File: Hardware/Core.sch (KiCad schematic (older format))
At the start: 12 parts

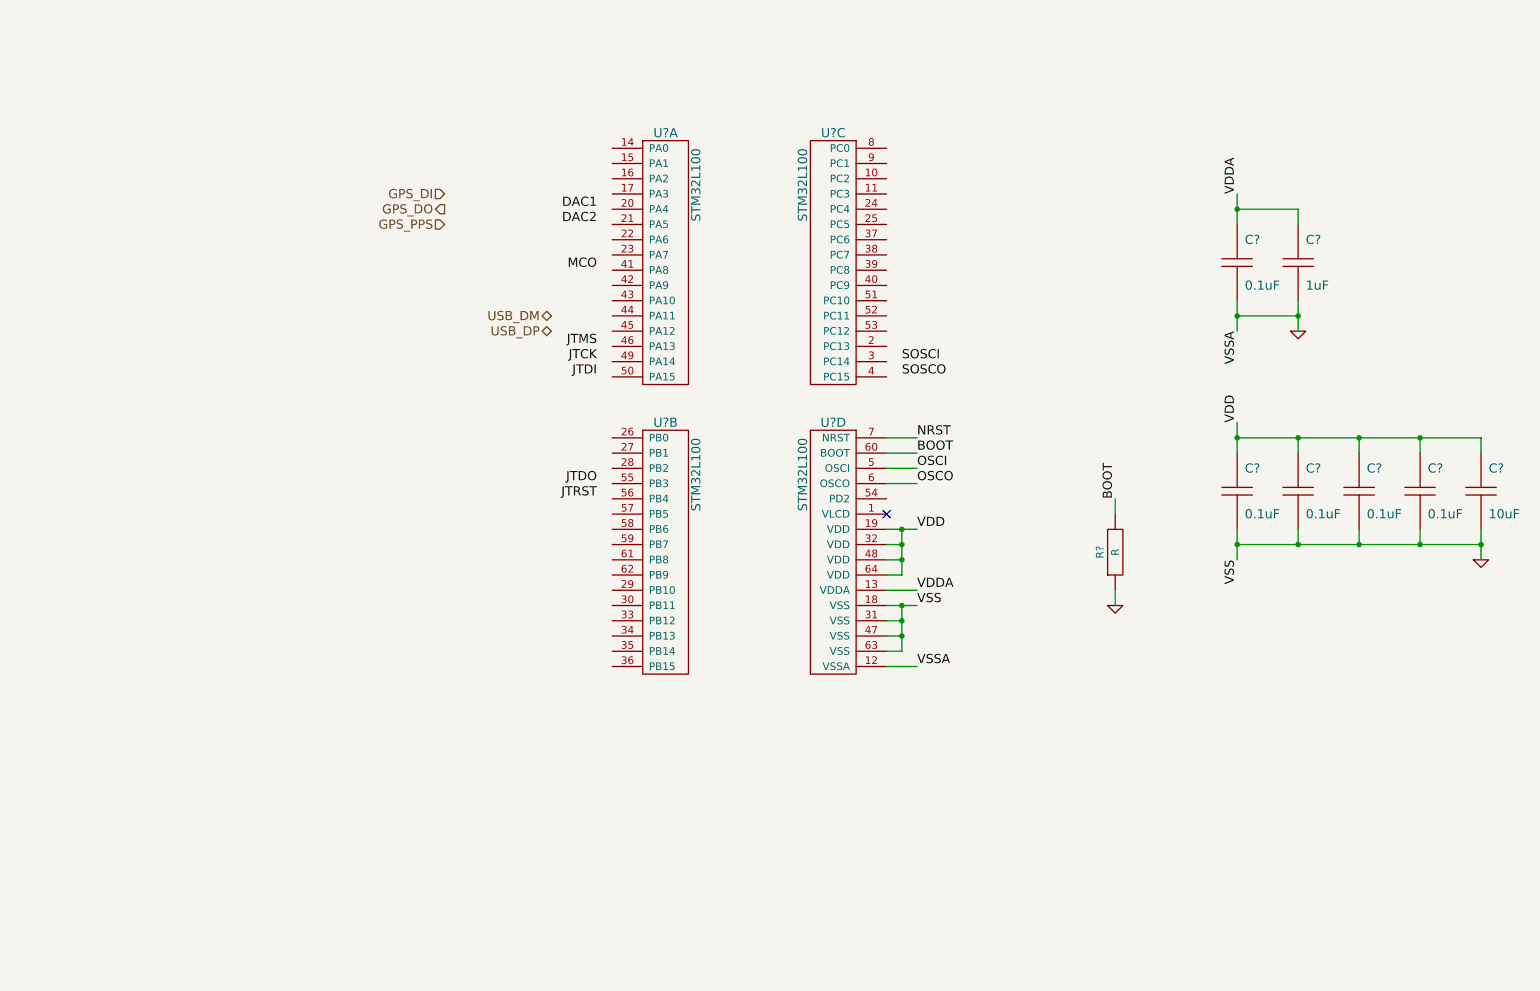
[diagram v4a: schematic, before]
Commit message: Add programming connector to core
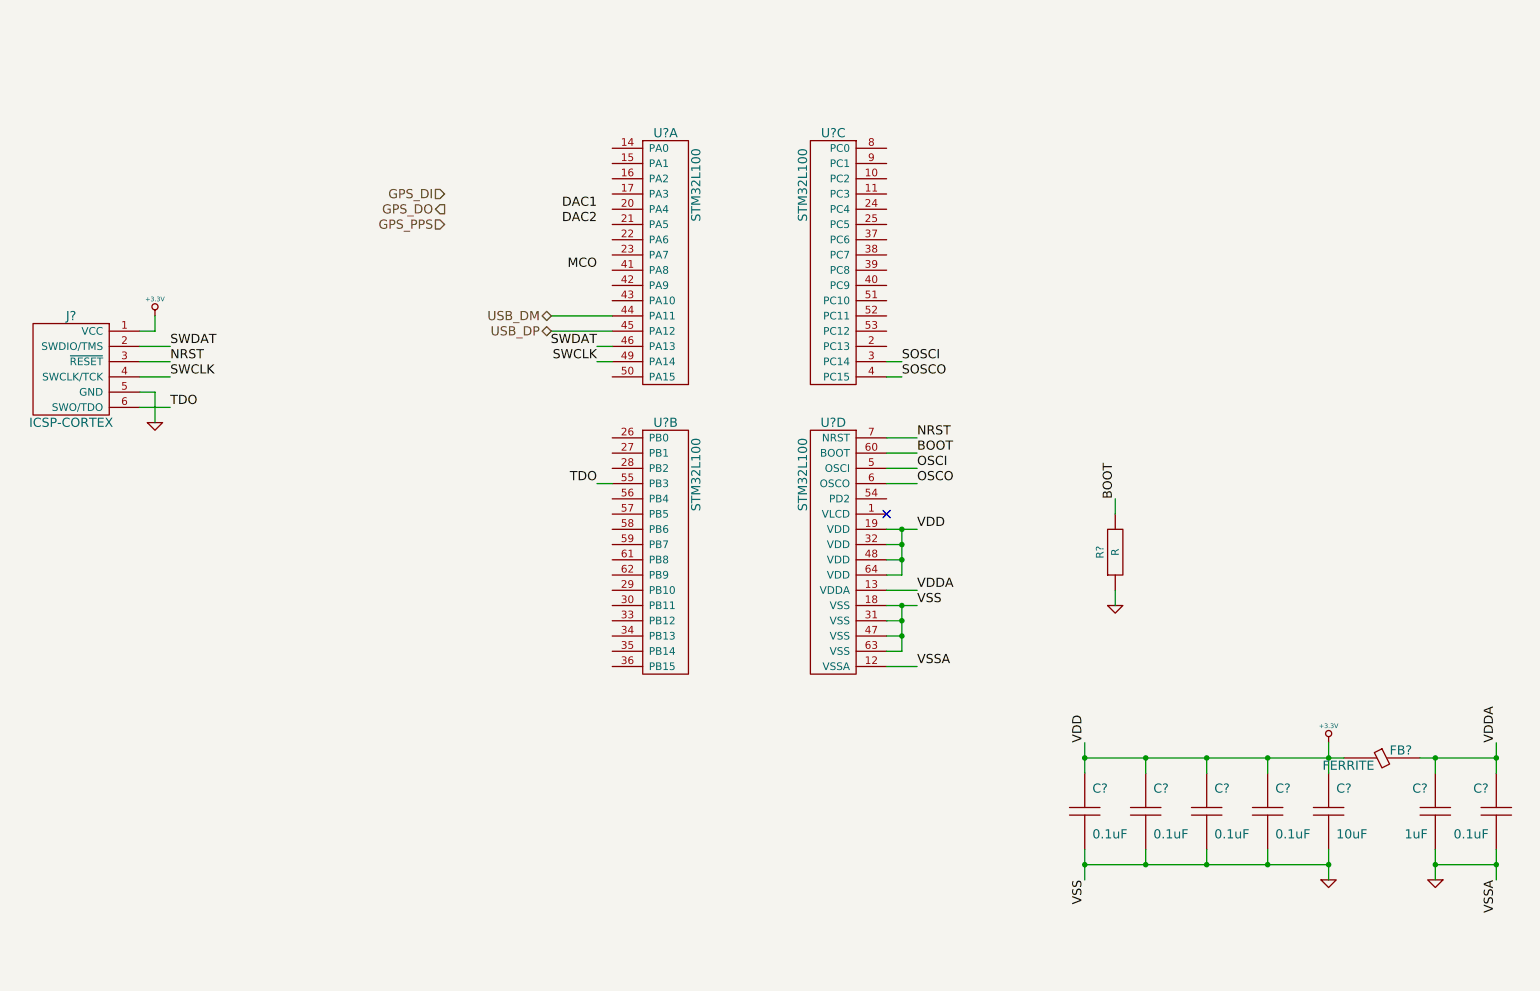
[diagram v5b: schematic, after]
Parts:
- added FB?: FERRITE, ~, symbol FERRITE
- added J?: ICSP-CORTEX, symbol ICSP-CORTEX
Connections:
- net GND: now also J?.5 (GND)
- net NRST: now also J?.3 (~RESET)
- net SOSCI: now also U?.3 (PC14)
- net SOSCO: now also U?.4 (PC15)
- net USB_DM: now also U?.44 (PA11)
- net USB_DP: now also U?.45 (PA12)
- net VDDA: now also FB?.1
- net SWDAT: now reaches U?.46 (PA13)
- net SWDAT: now also J?.2 (SWDIO/TMS)
- net SWCLK: now reaches U?.49 (PA14)
- net SWCLK: now also J?.4 (SWCLK/TCK)
- net TDO: now reaches U?.55 (PB3)
- net TDO: now also J?.6 (SWO/TDO)
- net VDD renamed +3.3V
- net +3.3V: now also FB?.2, J?.1 (VCC)
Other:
- moved on the sheet: C?

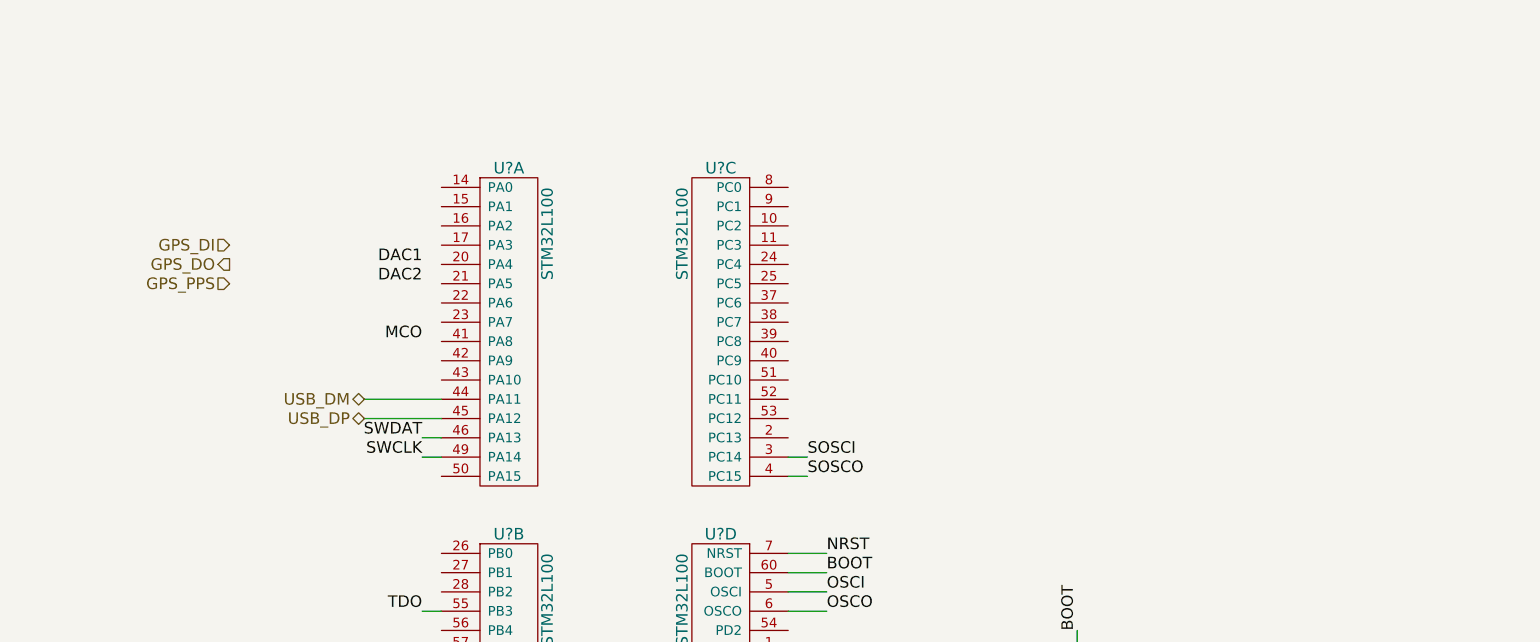
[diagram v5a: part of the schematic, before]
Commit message: Add crystals and connect pins
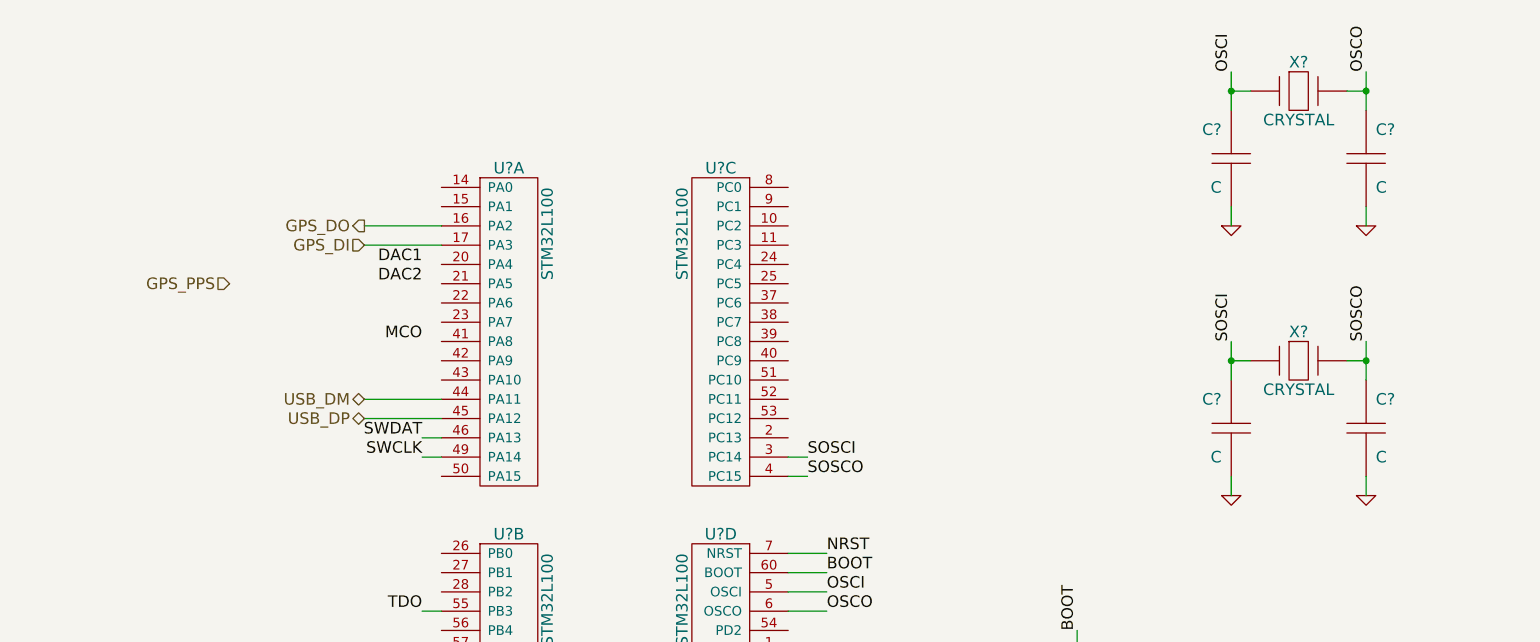
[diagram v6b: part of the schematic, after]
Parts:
- added C? (x4): C, ~, symbol C
- added X? (x2): CRYSTAL, ~, symbol CRYSTAL
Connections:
- net GND: now also C?.2, C?.2, C?.2, C?.2
- net GPS_DI: now also U?.17 (PA3)
- net GPS_DO: now also U?.16 (PA2)
- net OSCI: now also C?.1, X?.1
- net OSCO: now also C?.1, X?.2
- net SOSCI: now also C?.1, X?.1
- net SOSCO: now also C?.1, X?.2
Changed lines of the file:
@@
 Comment4 ""
 $EndDescr
-Text HLabel 3800 1900 0    60   Input ~ 0
+Text HLabel 4500 1900 0    60   Input ~ 0
 GPS_DI
-Text HLabel 3800 2000 0    60   Output ~ 0
+Text HLabel 4500 1800 0    60   Output ~ 0
 GPS_DO
 Text HLabel 3800 2100 0    60   Input ~ 0
@@
 Wire Wire Line
 	1900 2800 1800 2800
+Wire Wire Line
+	4500 1800 4900 1800
+Wire Wire Line
+	4500 1900 4900 1900
+$Comp
+L CRYSTAL X?
+U 1 1 53D85ADC
+P 9350 1100
+F 0 "X?" H 9350 1250 60  0000 C CNN
+F 1 "CRYSTAL" H 9350 950 60  0000 C CNN
+F 2 "~" H 9350 1100 60  0000 C CNN
+F 3 "~" H 9350 1100 60  0000 C CNN
+	1    9350 1100
+	1    0    0    -1
+$EndComp
+$Comp
+L C C?
+U 1 1 53D85AEB
+P 9000 1450
+F 0 "C?" H 9050 1600 60  0000 L CNN
+F 1 "C" H 9050 1300 60  0000 L CNN
+F 2 "~" H 9000 1450 60  0000 C CNN
+F 3 "~" H 9000 1450 60  0000 C CNN
+F 4 "V" H 8950 1300 60  0001 R CNN "Voltage"
+F 5 "D" H 8950 1600 60  0001 R CNN "Dielectric"
+	1    9000 1450
+	-1   0    0    -1
+$EndComp
+$Comp
+L C C?
+U 1 1 53D85B06
+P 9700 1450
+F 0 "C?" H 9750 1600 60  0000 L CNN
+F 1 "C" H 9750 1300 60  0000 L CNN
+F 2 "~" H 9700 1450 60  0000 C CNN
+F 3 "~" H 9700 1450 60  0000 C CNN
+F 4 "V" H 9650 1300 60  0001 R CNN "Voltage"
+F 5 "D" H 9650 1600 60  0001 R CNN "Dielectric"
+	1    9700 1450
+	1    0    0    -1
+$EndComp
+Text Label 9000 1000 1    60   ~ 0
+OSCI
+Text Label 9700 1000 1    60   ~ 0
+OSCO
+Wire Wire Line
+	9700 1000 9700 1200
+Wire Wire Line
+	9000 1000 9000 1200
+Wire Wire Line
+	9100 1100 9000 1100
+Connection ~ 9000 1100
+Wire Wire Line
+	9600 1100 9700 1100
+Connection ~ 9700 1100
+$Comp
+L GND #PWR?
+U 1 1 53D85C50
+P 9700 1800
+F 0 "#PWR?" H 9700 1800 30  0001 C CNN
+F 1 "GND" H 9700 1730 30  0001 C CNN
+F 2 "" H 9700 1800 60  0000 C CNN
+F 3 "" H 9700 1800 60  0000 C CNN
+	1    9700 1800
+	1    0    0    -1
+$EndComp
+$Comp
+L GND #PWR?
+U 1 1 53D85C5F
+P 9000 1800
+F 0 "#PWR?" H 9000 1800 30  0001 C CNN
+F 1 "GND" H 9000 1730 30  0001 C CNN
+F 2 "" H 9000 1800 60  0000 C CNN
+F 3 "" H 9000 1800 60  0000 C CNN
+	1    9000 1800
+	1    0    0    -1
+$EndComp
+Wire Wire Line
+	9000 1800 9000 1700
+Wire Wire Line
+	9700 1700 9700 1800
+$Comp
+L CRYSTAL X?
+U 1 1 53D85D0D
+P 9350 2500
+F 0 "X?" H 9350 2650 60  0000 C CNN
+F 1 "CRYSTAL" H 9350 2350 60  0000 C CNN
+F 2 "~" H 9350 2500 60  0000 C CNN
+F 3 "~" H 9350 2500 60  0000 C CNN
+	1    9350 2500
+	1    0    0    -1
+$EndComp
+$Comp
+L C C?
+U 1 1 53D85D15
+P 9000 2850
+F 0 "C?" H 9050 3000 60  0000 L CNN
+F 1 "C" H 9050 2700 60  0000 L CNN
+F 2 "~" H 9000 2850 60  0000 C CNN
+F 3 "~" H 9000 2850 60  0000 C CNN
+F 4 "V" H 8950 2700 60  0001 R CNN "Voltage"
+F 5 "D" H 8950 3000 60  0001 R CNN "Dielectric"
+	1    9000 2850
+	-1   0    0    -1
+$EndComp
+$Comp
+L C C?
+U 1 1 53D85D1D
+P 9700 2850
+F 0 "C?" H 9750 3000 60  0000 L CNN
+F 1 "C" H 9750 2700 60  0000 L CNN
+F 2 "~" H 9700 2850 60  0000 C CNN
+F 3 "~" H 9700 2850 60  0000 C CNN
+F 4 "V" H 9650 2700 60  0001 R CNN "Voltage"
+F 5 "D" H 9650 3000 60  0001 R CNN "Dielectric"
+	1    9700 2850
+	1    0    0    -1
+$EndComp
+Text Label 9000 2400 1    60   ~ 0
+SOSCI
+Text Label 9700 2400 1    60   ~ 0
+SOSCO
+Wire Wire Line
+	9700 2400 9700 2600
+Wire Wire Line
+	9000 2400 9000 2600
+Wire Wire Line
+	9100 2500 9000 2500
+Connection ~ 9000 2500
+Wire Wire Line
+	9600 2500 9700 2500
+Connection ~ 9700 2500
+$Comp
+L GND #PWR?
+U 1 1 53D85D2B
+P 9700 3200
+F 0 "#PWR?" H 9700 3200 30  0001 C CNN
+F 1 "GND" H 9700 3130 30  0001 C CNN
+F 2 "" H 9700 3200 60  0000 C CNN
+F 3 "" H 9700 3200 60  0000 C CNN
+	1    9700 3200
+	1    0    0    -1
+$EndComp
+$Comp
+L GND #PWR?
+U 1 1 53D85D31
+P 9000 3200
+F 0 "#PWR?" H 9000 3200 30  0001 C CNN
+F 1 "GND" H 9000 3130 30  0001 C CNN
+F 2 "" H 9000 3200 60  0000 C CNN
+F 3 "" H 9000 3200 60  0000 C CNN
+	1    9000 3200
+	1    0    0    -1
+$EndComp
+Wire Wire Line
+	9000 3200 9000 3100
+Wire Wire Line
+	9700 3100 9700 3200
 $EndSCHEMATC

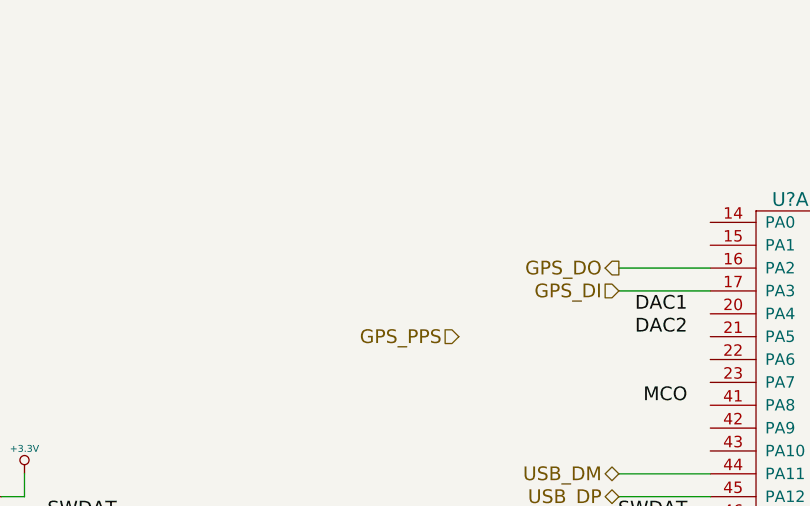
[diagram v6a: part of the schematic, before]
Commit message: Add gps enable connection
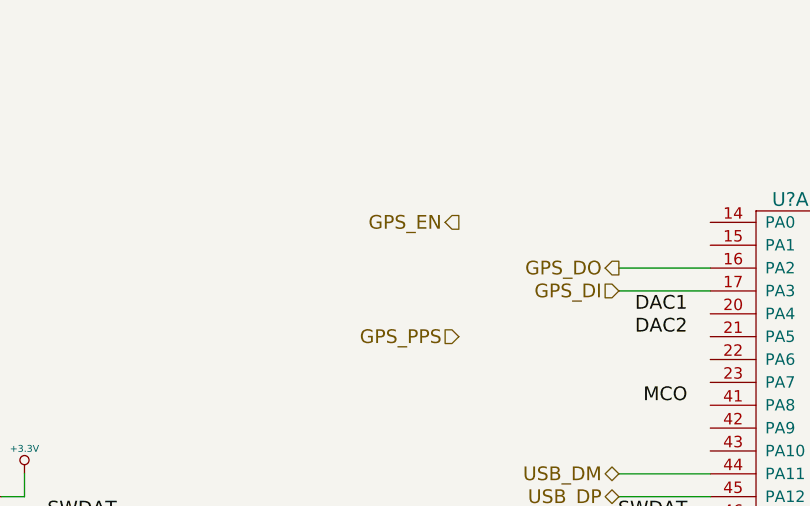
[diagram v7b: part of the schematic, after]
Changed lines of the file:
@@
 $Descr A4 11693 8268
 encoding utf-8
-Sheet 3 4
+Sheet 2 5
 Title "Aether - Pico Tracker"
-Date "30 jul 2014"
+Date "14 aug 2014"
 Rev "1"
 Comp "Aerodyne Labs"
@@
 Wire Wire Line
 	9700 3100 9700 3200
+Text HLabel 3800 1600 0    60   Output ~ 0
+GPS_EN
 $EndSCHEMATC

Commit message: Add LO control pins
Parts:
- R?: value R -> 10k
- X?: value CRYSTAL -> 32.768k
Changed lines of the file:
@@
 Sheet 2 5
 Title "Aether - Pico Tracker"
-Date "14 aug 2014"
+Date "15 aug 2014"
 Rev "1"
 Comp "Aerodyne Labs"
@@
 P 8200 4250
 F 0 "R?" H 8200 4350 50  0000 C CNN
-F 1 "R" H 8200 4250 50  0000 C CNN
+F 1 "10k" H 8200 4250 50  0000 C CNN
 F 2 "~" H 8200 4250 60  0000 C CNN
 F 3 "~" H 8200 4250 60  0000 C CNN
@@
 P 9350 2500
 F 0 "X?" H 9350 2650 60  0000 C CNN
-F 1 "CRYSTAL" H 9350 2350 60  0000 C CNN
+F 1 "32.768k" H 9350 2350 60  0000 C CNN
 F 2 "~" H 9350 2500 60  0000 C CNN
 F 3 "~" H 9350 2500 60  0000 C CNN
@@
 Text HLabel 3800 1600 0    60   Output ~ 0
 GPS_EN
+Text HLabel 4200 5900 2    60   Output ~ 0
+Mod
+Text Label 3900 5900 2    60   ~ 0
+DAC1
+Text HLabel 4200 5800 2    60   Output ~ 0
+LO_EN
 $EndSCHEMATC
